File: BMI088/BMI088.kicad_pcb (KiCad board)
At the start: 2 copper layers, 16.7 x 14 mm, 5 parts, among them J3 Conn_01x05_Pin, J4 Conn_01x05_Pin, U2 BMI088

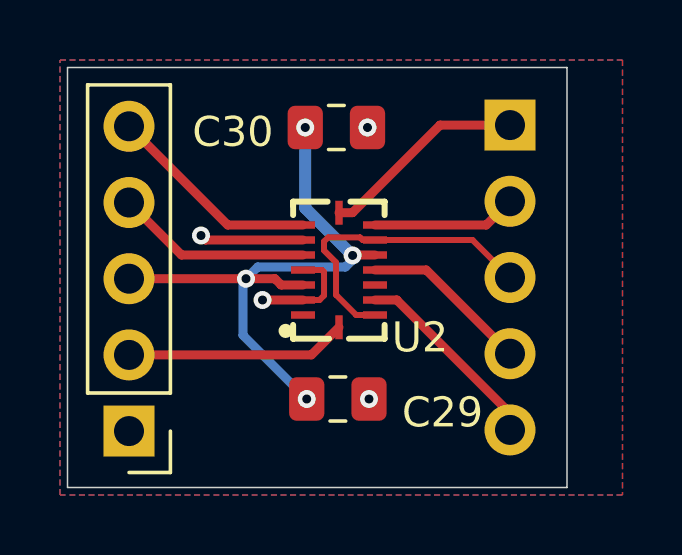
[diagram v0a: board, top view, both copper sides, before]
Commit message: add silkscreen
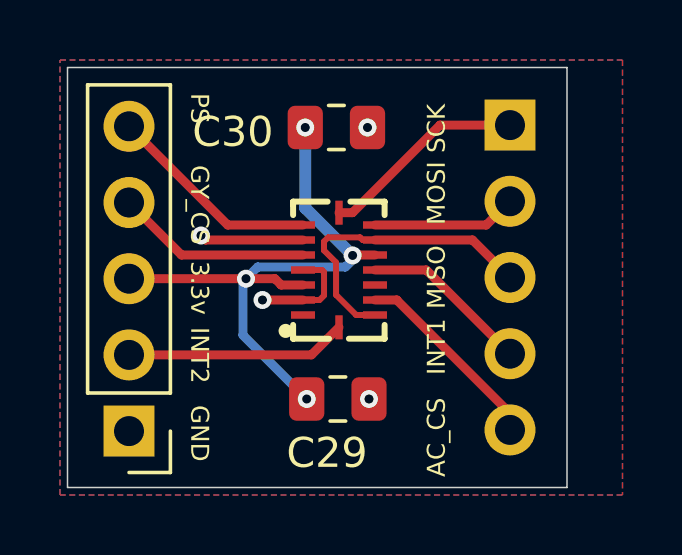
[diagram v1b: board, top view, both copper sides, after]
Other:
- board text added: "3.3v"
- board text added: "AC_CS"
- board text added: "GND"
- board text added: "GY_CS"
- board text added: "INT1"
- board text added: "INT2"
- board text added: "MISO"
- board text added: "MOSI"
- board text added: "PS"
- board text added: "SCK"
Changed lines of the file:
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@@
 		(tags "capacitor handsolder")
 		(property "Reference" "C29"
-			(at 3.4875 0.45 0)
+			(at -0.3625 1.8 0)
 			(layer "F.SilkS")
 			(effects
@@
 			(at 2.7 2.25 0)
 			(layer "F.SilkS")
+			(hide yes)
 			(effects
 				(font
@@
 		(layer "Edge.Cuts")
 	)
+	(gr_text "3.3v"
+		(at 161.8 87.2 270)
+		(layer "F.SilkS")
+		(effects
+			(font
+				(size 0.6 0.6)
+				(thickness 0.1)
+			)
+			(justify left bottom)
+		)
+	)
+	(gr_text "MISO"
+		(at 170.4 88.8 90)
+		(layer "F.SilkS")
+		(effects
+			(font
+				(size 0.6 0.6)
+				(thickness 0.1)
+			)
+			(justify left bottom)
+		)
+	)
+	(gr_text "AC_CS"
+		(at 170.4 94.4 90)
+		(layer "F.SilkS")
+		(effects
+			(font
+				(size 0.6 0.6)
+				(thickness 0.1)
+			)
+			(justify left bottom)
+		)
+	)
+	(gr_text "INT2"
+		(at 161.8 89.4 270)
+		(layer "F.SilkS")
+		(effects
+			(font
+				(size 0.6 0.6)
+				(thickness 0.1)
+			)
+			(justify left bottom)
+		)
+	)
+	(gr_text "SCK"
+		(at 170.4 83.6 90)
+		(layer "F.SilkS")
+		(effects
+			(font
+				(size 0.6 0.6)
+				(thickness 0.1)
+			)
+			(justify left bottom)
+		)
+	)
+	(gr_text "MOSI"
+		(at 170.4 86 90)
+		(layer "F.SilkS")
+		(effects
+			(font
+				(size 0.6 0.6)
+				(thickness 0.1)
+			)
+			(justify left bottom)
+		)
+	)
+	(gr_text "GND"
+		(at 161.8 92 270)
+		(layer "F.SilkS")
+		(effects
+			(font
+				(size 0.6 0.6)
+				(thickness 0.1)
+			)
+			(justify left bottom)
+		)
+	)
+	(gr_text "GY_CS"
+		(at 161.8 84 270)
+		(layer "F.SilkS")
+		(effects
+			(font
+				(size 0.6 0.6)
+				(thickness 0.1)
+			)
+			(justify left bottom)
+		)
+	)
+	(gr_text "INT1"
+		(at 170.4 91 90)
+		(layer "F.SilkS")
+		(effects
+			(font
+				(size 0.6 0.6)
+				(thickness 0.1)
+			)
+			(justify left bottom)
+		)
+	)
+	(gr_text "PS"
+		(at 161.8 81.6 270)
+		(layer "F.SilkS")
+		(effects
+			(font
+				(size 0.6 0.6)
+				(thickness 0.1)
+			)
+			(justify left bottom)
+		)
+	)
 	(segment
 		(start 166.151 88.5)
@@
 	)
 	(segment
+		(start 166.3 86.846929)
+		(end 166.3 86.55)
+		(width 0.2)
+		(layer "F.Cu")
+		(net 5)
+	)
+	(segment
+		(start 166.702 88.329)
+		(end 166.702 87.4079)
+		(width 0.2)
+		(layer "F.Cu")
+		(net 5)
+	)
+	(segment
+		(start 166.702 87.4079)
+		(end 166.7 87.4059)
+		(width 0.2)
+		(layer "F.Cu")
+		(net 5)
+	)
+	(segment
+		(start 166.7 87.4059)
+		(end 166.7 87.246929)
+		(width 0.2)
+		(layer "F.Cu")
+		(net 5)
+	)
+	(segment
 		(start 168 86.5)
 		(end 171.25 86.5)
-		(width 0.2)
-		(layer "F.Cu")
-		(net 5)
-	)
-	(segment
-		(start 166.3 86.846929)
-		(end 166.3 86.55)
-		(width 0.2)
-		(layer "F.Cu")
-		(net 5)
-	)
-	(segment
-		(start 166.702 88.329)
-		(end 166.702 87.4079)
-		(width 0.2)
-		(layer "F.Cu")
-		(net 5)
-	)
-	(segment
-		(start 166.702 87.4079)
-		(end 166.7 87.4059)
-		(width 0.2)
-		(layer "F.Cu")
-		(net 5)
-	)
-	(segment
-		(start 166.7 87.4059)
-		(end 166.7 87.246929)
-		(width 0.2)
+		(width 0.3)
 		(layer "F.Cu")
 		(net 5)
@@
 	)
 	(segment
+		(start 171.25 86.5)
+		(end 172.5 87.75)
+		(width 0.3)
+		(layer "F.Cu")
+		(net 5)
+	)
+	(segment
 		(start 166.3 86.55)
 		(end 166.43624 86.41376)
 		(width 0.2)
 		(layer "F.Cu")
-		(net 5)
-	)
-	(segment
-		(start 171.25 86.5)
-		(end 172.5 87.75)
-		(width 0.2)
-		(layer "F.Cu")
